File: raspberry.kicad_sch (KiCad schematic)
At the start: 7 parts

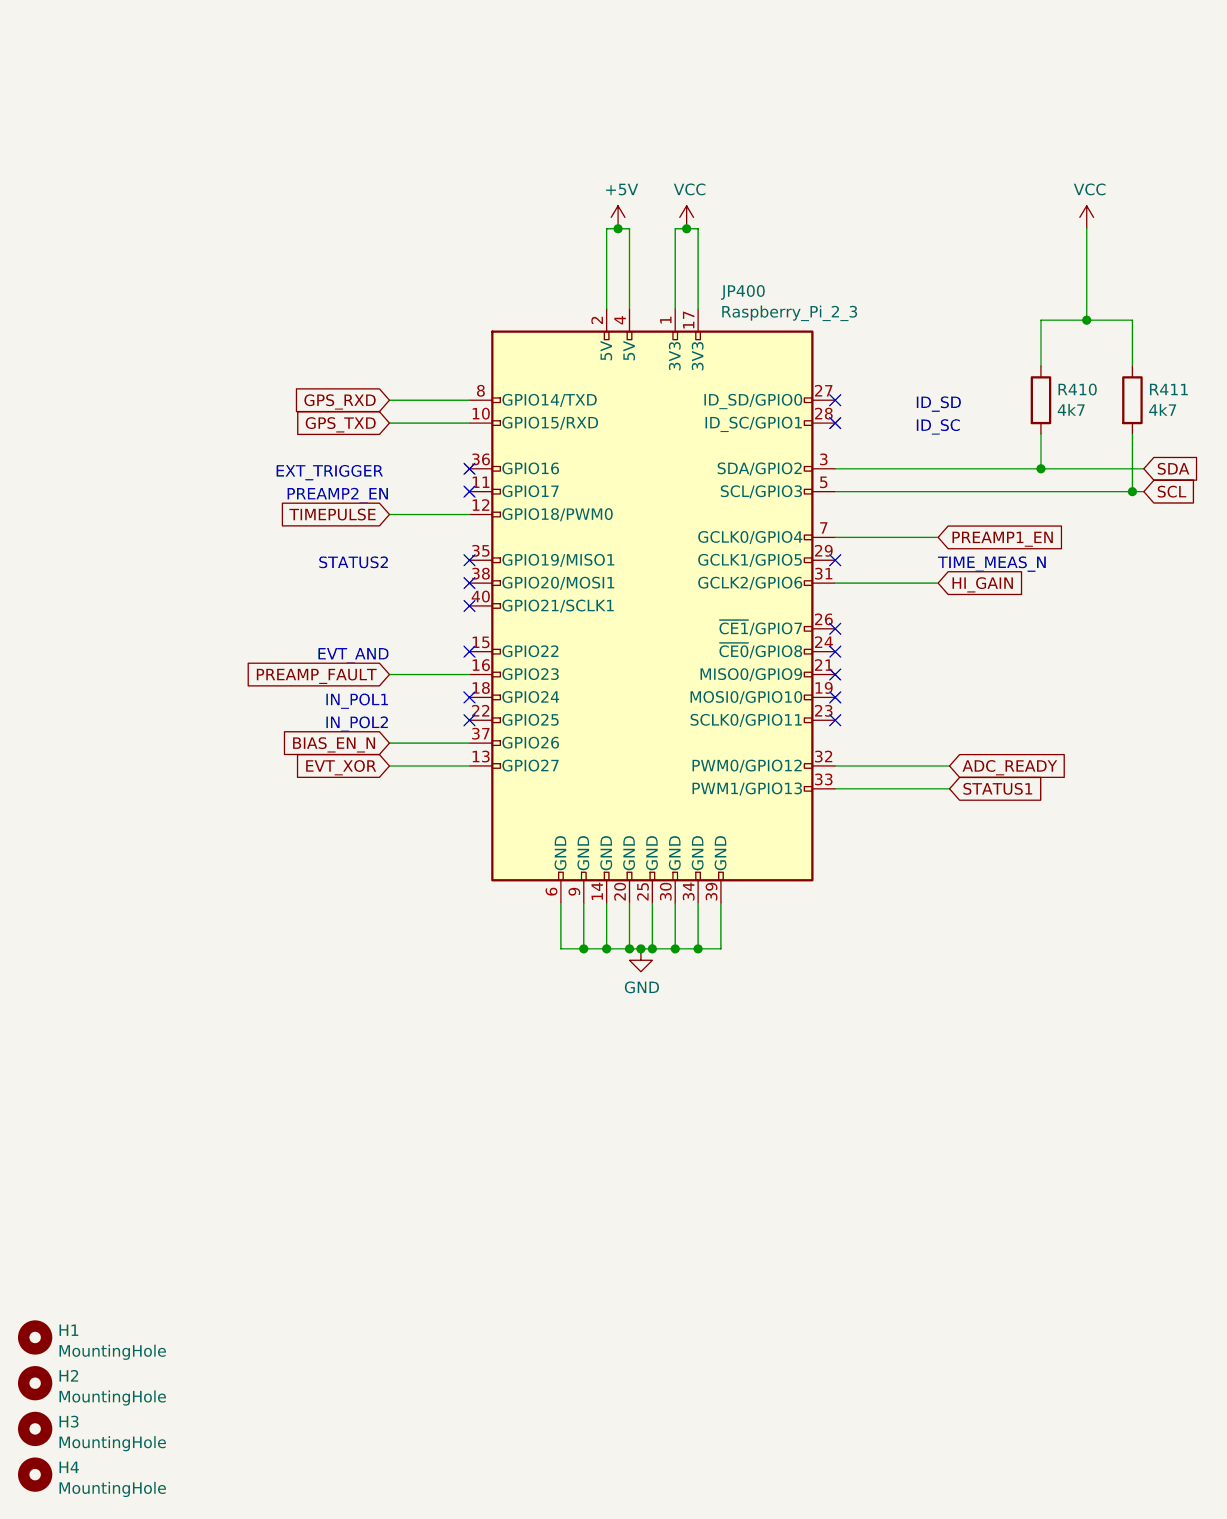
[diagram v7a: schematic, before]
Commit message: Refactored schematic to better show relationship in main schematic
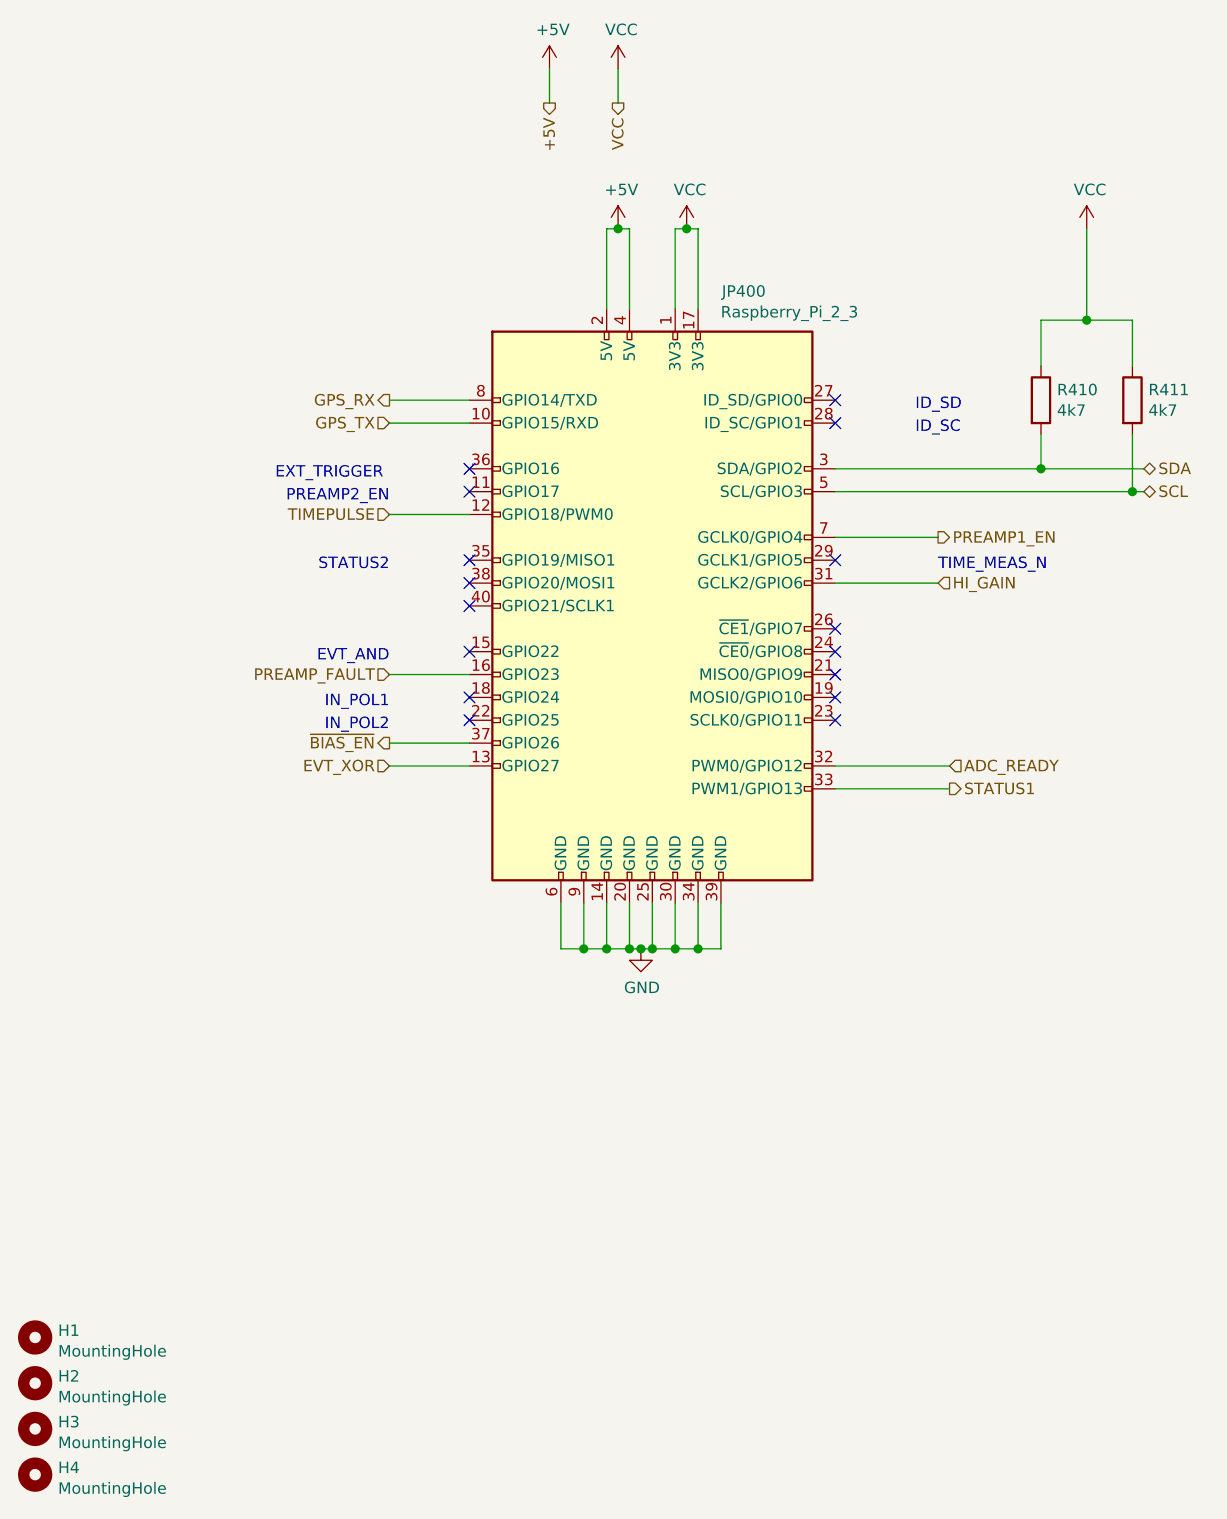
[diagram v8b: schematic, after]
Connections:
- net BIAS_EN_N renamed ~{BIAS_EN}
- net GPS_RXD renamed GPS_RX
- net GPS_TXD renamed GPS_TX
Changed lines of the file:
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@@
-(kicad_sch (version 20210406) (generator eeschema)
+(kicad_sch (version 20210621) (generator eeschema)
   (paper "A4")
   (junction (at 147.32 129.54) (diameter 1.016) (color 0 0 0 0))
@@
     (stroke (width 0) (type solid) (color 0 0 0 0))
   )
+  (wire (pts (xy 143.51 31.75) (xy 143.51 35.56))
+    (stroke (width 0) (type default) (color 0 0 0 0))
+  )
   (wire (pts (xy 144.78 124.46) (xy 144.78 129.54))
     (stroke (width 0) (type solid) (color 0 0 0 0))
@@
     (stroke (width 0) (type solid) (color 0 0 0 0))
   )
+  (wire (pts (xy 151.13 31.75) (xy 151.13 35.56))
+    (stroke (width 0) (type default) (color 0 0 0 0))
+  )
   (wire (pts (xy 151.13 49.53) (xy 152.4 49.53))
     (stroke (width 0) (type solid) (color 0 0 0 0))
@@
     (effects (font (size 1.27 1.27)) (justify left bottom))
   )
-  (global_label "GPS_RXD" (shape input) (at 125.73 68.58 180)
-    (effects (font (size 1.27 1.27)) (justify right))
-    (property "Intersheet References" "${INTERSHEET_REFS}" (id 0) (at 113.3262 68.5006 0)
-      (effects (font (size 1.27 1.27)) (justify right) hide)
-    )
-  )
-  (global_label "GPS_TXD" (shape input) (at 125.73 71.12 180)
-    (effects (font (size 1.27 1.27)) (justify right))
-    (property "Intersheet References" "${INTERSHEET_REFS}" (id 0) (at 113.6286 71.0406 0)
-      (effects (font (size 1.27 1.27)) (justify right) hide)
-    )
-  )
-  (global_label "TIMEPULSE" (shape input) (at 125.73 81.28 180)
-    (effects (font (size 1.27 1.27)) (justify right))
-    (property "Intersheet References" "${INTERSHEET_REFS}" (id 0) (at 111.6329 81.2006 0)
-      (effects (font (size 1.27 1.27)) (justify right) hide)
-    )
-  )
-  (global_label "PREAMP_FAULT" (shape input) (at 125.73 99.06 180)
-    (effects (font (size 1.27 1.27)) (justify right))
-    (property "Intersheet References" "${INTERSHEET_REFS}" (id 0) (at 107.8229 98.9806 0)
-      (effects (font (size 1.27 1.27)) (justify right) hide)
-    )
-  )
-  (global_label "BIAS_EN_N" (shape input) (at 125.73 106.68 180)
-    (effects (font (size 1.27 1.27)) (justify right))
-    (property "Intersheet References" "${INTERSHEET_REFS}" (id 0) (at 111.8748 106.6006 0)
-      (effects (font (size 1.27 1.27)) (justify right) hide)
-    )
-  )
-  (global_label "EVT_XOR" (shape input) (at 125.73 109.22 180)
-    (effects (font (size 1.27 1.27)) (justify right))
-    (property "Intersheet References" "${INTERSHEET_REFS}" (id 0) (at 113.81 109.1406 0)
-      (effects (font (size 1.27 1.27)) (justify right) hide)
-    )
-  )
-  (global_label "PREAMP1_EN" (shape input) (at 186.69 83.82 0)
-    (effects (font (size 1.27 1.27)) (justify left))
-    (property "Intersheet References" "${INTERSHEET_REFS}" (id 0) (at 202.7828 83.7406 0)
-      (effects (font (size 1.27 1.27)) (justify left) hide)
-    )
-  )
-  (global_label "HI_GAIN" (shape input) (at 186.69 88.9 0)
-    (effects (font (size 1.27 1.27)) (justify left))
-    (property "Intersheet References" "${INTERSHEET_REFS}" (id 0) (at 197.8238 88.9794 0)
-      (effects (font (size 1.27 1.27)) (justify left) hide)
-    )
-  )
-  (global_label "ADC_READY" (shape input) (at 187.96 109.22 0)
-    (effects (font (size 1.27 1.27)) (justify left))
-    (property "Intersheet References" "${INTERSHEET_REFS}" (id 0) (at 202.3595 109.1406 0)
-      (effects (font (size 1.27 1.27)) (justify left) hide)
-    )
-  )
-  (global_label "STATUS1" (shape input) (at 187.96 111.76 0)
-    (effects (font (size 1.27 1.27)) (justify left))
-    (property "Intersheet References" "${INTERSHEET_REFS}" (id 0) (at 199.88 111.6806 0)
-      (effects (font (size 1.27 1.27)) (justify left) hide)
-    )
-  )
-  (global_label "SDA" (shape input) (at 209.55 76.2 0)
-    (effects (font (size 1.27 1.27)) (justify left))
-    (property "Intersheet References" "${INTERSHEET_REFS}" (id 0) (at 217.0552 76.1206 0)
-      (effects (font (size 1.27 1.27)) (justify left) hide)
-    )
-  )
-  (global_label "SCL" (shape input) (at 209.55 78.74 0)
-    (effects (font (size 1.27 1.27)) (justify left))
-    (property "Intersheet References" "${INTERSHEET_REFS}" (id 0) (at 216.9947 78.6606 0)
-      (effects (font (size 1.27 1.27)) (justify left) hide)
-    )
+  (hierarchical_label "GPS_RX" (shape output) (at 125.73 68.58 180)
+    (effects (font (size 1.27 1.27)) (justify right))
+  )
+  (hierarchical_label "GPS_TX" (shape input) (at 125.73 71.12 180)
+    (effects (font (size 1.27 1.27)) (justify right))
+  )
+  (hierarchical_label "TIMEPULSE" (shape input) (at 125.73 81.28 180)
+    (effects (font (size 1.27 1.27)) (justify right))
+  )
+  (hierarchical_label "PREAMP_FAULT" (shape input) (at 125.73 99.06 180)
+    (effects (font (size 1.27 1.27)) (justify right))
+  )
+  (hierarchical_label "~{BIAS_EN}" (shape output) (at 125.73 106.68 180)
+    (effects (font (size 1.27 1.27)) (justify right))
+  )
+  (hierarchical_label "EVT_XOR" (shape input) (at 125.73 109.22 180)
+    (effects (font (size 1.27 1.27)) (justify right))
+  )
+  (hierarchical_label "+5V" (shape output) (at 143.51 35.56 270)
+    (effects (font (size 1.27 1.27)) (justify right))
+  )
+  (hierarchical_label "VCC" (shape output) (at 151.13 35.56 270)
+    (effects (font (size 1.27 1.27)) (justify right))
+  )
+  (hierarchical_label "PREAMP1_EN" (shape output) (at 186.69 83.82 0)
+    (effects (font (size 1.27 1.27)) (justify left))
+  )
+  (hierarchical_label "HI_GAIN" (shape input) (at 186.69 88.9 0)
+    (effects (font (size 1.27 1.27)) (justify left))
+  )
+  (hierarchical_label "ADC_READY" (shape input) (at 187.96 109.22 0)
+    (effects (font (size 1.27 1.27)) (justify left))
+  )
+  (hierarchical_label "STATUS1" (shape output) (at 187.96 111.76 0)
+    (effects (font (size 1.27 1.27)) (justify left))
+  )
+  (hierarchical_label "SDA" (shape bidirectional) (at 209.55 76.2 0)
+    (effects (font (size 1.27 1.27)) (justify left))
+  )
+  (hierarchical_label "SCL" (shape bidirectional) (at 209.55 78.74 0)
+    (effects (font (size 1.27 1.27)) (justify left))
+  )
+  (symbol (lib_id "power:+5V") (at 143.51 31.75 0) (unit 1)
+    (in_bom yes) (on_board yes)
+    (property "Reference" "#PWR0223" (id 0) (at 143.51 35.56 0)
+      (effects (font (size 1.27 1.27)) hide)
+    )
+    (property "Value" "+5V" (id 1) (at 143.8783 27.4256 0))
+    (property "Footprint" "" (id 2) (at 143.51 31.75 0)
+      (effects (font (size 1.27 1.27)) hide)
+    )
+    (property "Datasheet" "" (id 3) (at 143.51 31.75 0)
+      (effects (font (size 1.27 1.27)) hide)
+    )
+    (pin "1")
+  )
+  (symbol (lib_id "power:VCC") (at 151.13 31.75 0) (unit 1)
+    (in_bom yes) (on_board yes)
+    (property "Reference" "#PWR0224" (id 0) (at 151.13 35.56 0)
+      (effects (font (size 1.27 1.27)) hide)
+    )
+    (property "Value" "VCC" (id 1) (at 151.4983 27.4256 0))
+    (property "Footprint" "" (id 2) (at 151.13 31.75 0)
+      (effects (font (size 1.27 1.27)) hide)
+    )
+    (property "Datasheet" "" (id 3) (at 151.13 31.75 0)
+      (effects (font (size 1.27 1.27)) hide)
+    )
+    (pin "1")
   )
   (symbol (lib_id "power:+5V") (at 151.13 49.53 0) (unit 1)
